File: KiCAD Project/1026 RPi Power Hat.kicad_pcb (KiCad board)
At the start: 4 copper layers, 85 x 56.5 mm, 131 parts, among them J1 S2B-XH-A-1, J2 B2B-XH-A(LF)(SN), J3 ESW-120-33-G-D, J4 USB1030-GF-P-B-B, J5 USB1035-GF-P-0-B-B, J6 USB1035-GF-P-0-B-B, M1 CFM-2507CF-050-089, P1 DW_PCB_Logo, P2 Raspberry Pi HAT+ Designator, Q1 BUK6D120-60PX, U1 LM64440APPQRYFRQ1, U10 USBLC6-2P6, U11 USBLC6-2P6, U12 USBLC6-2P6, U2 TLV75511PDQNR, U3 TLV75533PDQNR, U4 TUSB4041IPAPR, U5 TPS2561DRCR, U6 TPS2561DRCR, U7 CAT24C32HU4I-GT3, U8 USBLC6-2P6, U9 USBLC6-2P6, Y1 ECS-2520MV-240-BL-TR

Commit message: v1.0.0 RC2
Build candidate 2
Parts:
- M1: value CFM-2507CF-050-089 -> CFM-2510B-070-140; footprint DW_Mechanical:[Fan] SameSky CFM-2507CF-050-089 -> DW_Mechanical:[Fan] SameSky CFM-2510B-070-140
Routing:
- net /USB Hub/USB_Vbus: track 75.2 -> 78.9 mm, vias 1 -> 3
- net /5V Regulator/5V: track 15.4 -> 14.4 mm
- net GND: vias 92 -> 91
- added copper zone on In2.Cu, net /5V Regulator/24V
- removed copper zone on B.Cu, net /5V Regulator/24V
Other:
- board text added: "Fault"
- board text removed: "OC Fault"

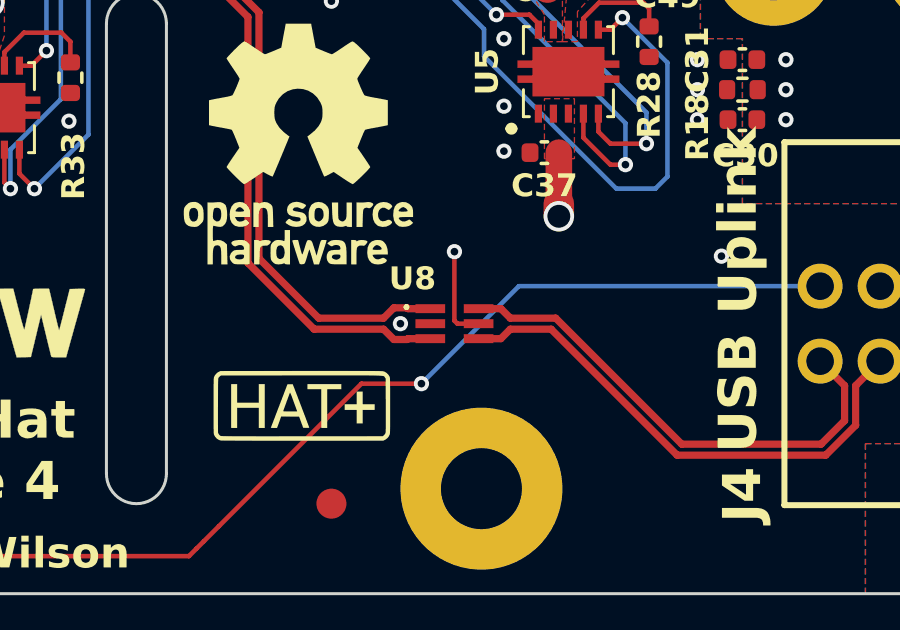
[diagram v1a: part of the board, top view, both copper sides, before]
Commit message: v1.0.0 RC3
Minor change to upstream USB port to connect Vbus to ESD protection vice on-board 5V.
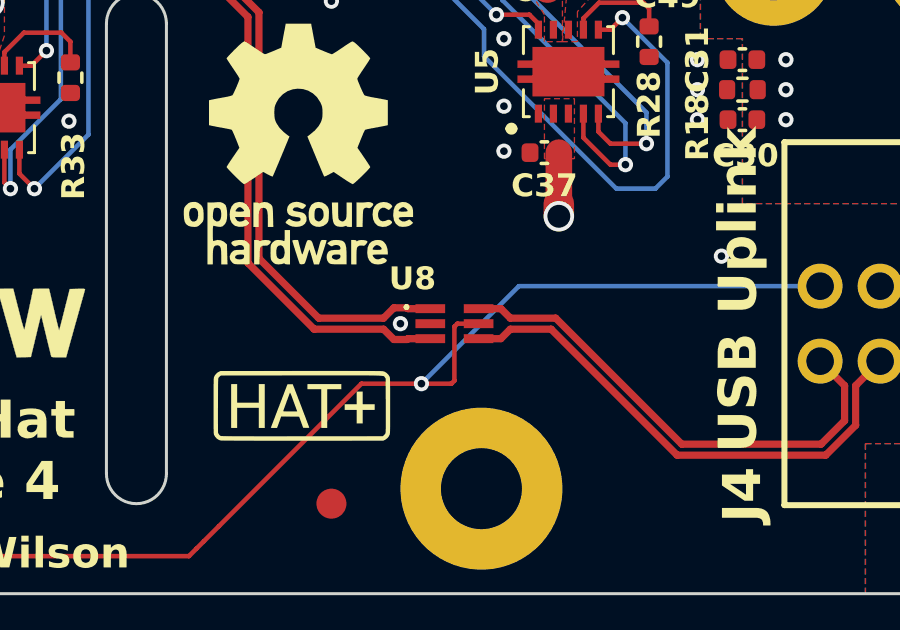
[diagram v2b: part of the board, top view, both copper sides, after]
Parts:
- C12: value GRM0225C1C100FA03L -> VJ0402A100GXJCW1BC
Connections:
- U8 pad 5: /5V Regulator/5V -> /USB Hub/USB_Vbus
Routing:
- net /USB Hub/USB_Vbus: track 78.9 -> 82.7 mm
- net /5V Regulator/5V: track 14.4 -> 11.2 mm, vias 26 -> 25
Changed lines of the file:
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@@
 		(title "1026 RPi Power Hat")
 		(date "2025-04-13")
-		(rev "1")
+		(rev "1.0.0 RC3")
 		(company "Dan Wilson")
 		(comment 1 "Copyright © 2025")
@@
 			)
 		)
-		(property "Spec" ""
+		(property "Spec" "CAT24C32HU4I-GT3"
 			(at 0 0 0)
 			(unlocked yes)
@@
 			)
 		)
-		(property "Value" "GRM0225C1C100FA03L"
+		(property "Value" "VJ0402A100GXJCW1BC"
 			(at 0 1.16 90)
 			(layer "F.Fab")
@@
 			)
 		)
-		(property "Datasheet" "https://www.mouser.com/datasheet/2/281/GRM0225C1C100FA03_01A-1978859.pdf"
+		(property "Datasheet" "https://www.vishay.com/doc?28548"
 			(at 0 0 270)
 			(unlocked yes)
@@
 			)
 		)
-		(property "Height" "0.25"
+		(property "Height" "0.5"
 			(at 0 0 270)
 			(unlocked yes)
@@
 			)
 		)
-		(property "Manufacturer_Name" "Murata"
+		(property "Manufacturer_Name" "Vishay"
 			(at 0 0 270)
 			(unlocked yes)
@@
 			)
 		)
-		(property "Manufacturer_Part_Number" "GRM0225C1C100FA03L"
+		(property "Manufacturer_Part_Number" "VJ0402A100GXJCW1BC"
 			(at 0 0 270)
 			(unlocked yes)
@@
 			)
 		)
-		(property "Mouser Part Number" "81-GRM0225C1C100FA03"
+		(property "Mouser Part Number" "77-VJ0402A100GXJCBC"
 			(at 0 0 270)
 			(unlocked yes)
@@
 			)
 		)
-		(property "Mouser Price/Stock" "https://www.mouser.com/ProductDetail/Murata-Electronics/GRM0225C1C100FA03L?qs=rrS6PyfT74dMR%2FKublCCEA%3D%3D"
+		(property "Mouser Price/Stock" "https://www.mouser.com/ProductDetail/77-VJ0402A100GXJCBC"
 			(at 0 0 270)
 			(unlocked yes)
@@
 			)
 		)
+		(property "Mouser Price/Stock" "https://www.mouser.com/ProductDetail/STMicroelectronics/USBLC6-2P6?qs=6ARB0lp6jlViGcbUSvj1Mw%3D%3D"
+			(at 0 0 270)
+			(unlocked yes)
+			(layer "F.Fab")
+			(hide yes)
+			(effects
+				(font
+					(size 1 1)
+					(thickness 0.15)
+				)
+			)
+		)
 		(sheetname "/USB ESD Protection/")
 		(sheetfile "USB ESD Protection.kicad_sch")
@@
 			)
 		)
+		(property "Spec" "TPS2561DRCR"
+			(at 0 0 90)
+			(unlocked yes)
+			(layer "F.Fab")
+			(hide yes)
+			(effects
+				(font
+					(size 1 1)
+					(thickness 0.15)
+				)
+			)
+		)
 		(sheetname "/USB Power Control/")
 		(sheetfile "USB Power Control.kicad_sch")
@@
 			)
 		)
+		(property "Mouser Price/Stock" "https://www.mouser.com/ProductDetail/STMicroelectronics/USBLC6-2P6?qs=6ARB0lp6jlViGcbUSvj1Mw%3D%3D"
+			(at 0 0 315)
+			(unlocked yes)
+			(layer "F.Fab")
+			(hide yes)
+			(effects
+				(font
+					(size 1 1)
+					(thickness 0.15)
+				)
+			)
+		)
 		(sheetname "/USB ESD Protection/")
 		(sheetfile "USB ESD Protection.kicad_sch")
@@
 			)
 		)
+		(property "Spec" "TPS2561DRCR"
+			(at 0 0 90)
+			(unlocked yes)
+			(layer "F.Fab")
+			(hide yes)
+			(effects
+				(font
+					(size 1 1)
+					(thickness 0.15)
+				)
+			)
+		)
 		(sheetname "/USB Power Control/")
 		(sheetfile "USB Power Control.kicad_sch")
@@
 			)
 		)
+		(property "Mouser Price/Stock" "https://www.mouser.com/ProductDetail/STMicroelectronics/USBLC6-2P6?qs=6ARB0lp6jlViGcbUSvj1Mw%3D%3D"
+			(at 0 0 315)
+			(unlocked yes)
+			(layer "F.Fab")
+			(hide yes)
+			(effects
+				(font
+					(size 1 1)
+					(thickness 0.15)
+				)
+			)
+		)
 		(sheetname "/USB ESD Protection/")
 		(sheetfile "USB ESD Protection.kicad_sch")
@@
 			)
 		)
-		(property "Mouser Part Number" ""
+		(property "Mouser Part Number" "306-B2BXHALFSNP"
 			(at 0 0 270)
 			(unlocked yes)
@@
 			)
 		)
+		(property "Mouser Price/Stock" "https://www.mouser.com/ProductDetail/JST-Commercial/B2B-XH-ALFSN?qs=cdbOS8ANM9DdcSn9qRmfCw%3D%3D"
+			(at 0 0 270)
+			(unlocked yes)
+			(layer "F.Fab")
+			(hide yes)
+			(effects
+				(font
+					(size 1 1)
+					(thickness 0.15)
+				)
+			)
+		)
 		(sheetname "/Fan / Header / GPIO / EEPROM/")
 		(sheetfile "Fan Header and Fan.kicad_sch")
@@
 			)
 		)
+		(property "Mouser Price/Stock" "https://www.mouser.com/ProductDetail/STMicroelectronics/USBLC6-2P6?qs=6ARB0lp6jlViGcbUSvj1Mw%3D%3D"
+			(at 0 0 270)
+			(unlocked yes)
+			(layer "F.Fab")
+			(hide yes)
+			(effects
+				(font
+					(size 1 1)
+					(thickness 0.15)
+				)
+			)
+		)
 		(sheetname "/USB ESD Protection/")
 		(sheetfile "USB ESD Protection.kicad_sch")
@@
 			(size 0.3 0.99)
 			(layers "F.Cu" "F.Mask" "F.Paste")
-			(net 7 "/5V Regulator/5V")
+			(net 90 "/USB Hub/USB_Vbus")
 			(pinfunction "VBUS")
 			(pintype "passive")
@@
 			)
 		)
-		(property "Mouser Part Number" ""
+		(property "Mouser Part Number" "306-S2BXHA1LFSN"
 			(at 0 0 180)
 			(unlocked yes)
@@
 			)
 		)
+		(property "Mouser Price/Stock" "https://www.mouser.com/ProductDetail/JST-Commercial/S2B-XH-A-1LFSN?qs=QpmGXVUTftHhNeC%252BPQWeTw%3D%3D"
+			(at 0 0 180)
+			(unlocked yes)
+			(layer "F.Fab")
+			(hide yes)
+			(effects
+				(font
+					(size 1 1)
+					(thickness 0.15)
+				)
+			)
+		)
 		(sheetname "/Power Input/")
 		(sheetfile "Power Input.kicad_sch")
@@
 			)
 		)
+		(property "Spec" "ECS-2520MV-240-BL-TR"
+			(at 0 0 135)
+			(unlocked yes)
+			(layer "F.Fab")
+			(hide yes)
+			(effects
+				(font
+					(size 1 1)
+					(thickness 0.15)
+				)
+			)
+		)
 		(sheetname "/USB Power Control/")
 		(sheetfile "USB Power Control.kicad_sch")
@@
 			)
 		)
+		(property "Spec" "5V 7000RPM 25mm"
+			(at 0 0 180)
+			(unlocked yes)
+			(layer "F.Fab")
+			(hide yes)
+			(effects
+				(font
+					(size 1 1)
+					(thickness 0.15)
+				)
+			)
+		)
 		(sheetname "/Fan / Header / GPIO / EEPROM/")
 		(sheetfile "Fan Header and Fan.kicad_sch")
@@
 			)
 		)
+		(property "Mouser Price/Stock" "https://www.mouser.com/ProductDetail/STMicroelectronics/USBLC6-2P6?qs=6ARB0lp6jlViGcbUSvj1Mw%3D%3D"
+			(at 0 0 315)
+			(unlocked yes)
+			(layer "F.Fab")
+			(hide yes)
+			(effects
+				(font
+					(size 1 1)
+					(thickness 0.15)
+				)
+			)
+		)
 		(sheetname "/USB ESD Protection/")
 		(sheetfile "USB ESD Protection.kicad_sch")
@@
 			)
 		)
+		(property "Spec" "TUSB4041IPAPR"
+			(at 0 0 315)
+			(unlocked yes)
+			(layer "F.Fab")
+			(hide yes)
+			(effects
+				(font
+					(size 1 1)
+					(thickness 0.15)
+				)
+			)
+		)
 		(sheetname "/USB Hub/")
 		(sheetfile "USB Hub and Power Control.kicad_sch")
@@
 	)
 	(segment
-		(start 160.6992 141)
-		(end 160.6 140.9008)
-		(width 0.1524)
-		(layer "F.Cu")
-		(net 7)
-	)
-	(segment
 		(start 125.74 143.99)
 		(end 125.75 144)
@@
 	)
 	(segment
-		(start 160.6 140.9008)
-		(end 160.6 138.6)
-		(width 0.1524)
-		(layer "F.Cu")
-		(net 7)
-	)
-	(segment
 		(start 123 140.26)
 		(end 123 142.75)
@@
 		(net 7)
 	)
-	(segment
-		(start 161.405 141)
-		(end 160.6992 141)
-		(width 0.1524)
-		(layer "F.Cu")
-		(net 7)
-	)
 	(via
 		(at 123 142.75)
@@
 	)
 	(via
-		(at 160.6 138.6)
-		(size 0.508)
-		(drill 0.254)
-		(layers "F.Cu" "B.Cu")
-		(net 7)
-	)
-	(via
 		(at 121.5 130.25)
 		(size 0.508)
@@
 	)
 	(segment
+		(start 160.6992 141)
+		(end 161.405 141)
+		(width 0.1524)
+		(layer "F.Cu")
+		(net 90)
+	)
+	(segment
 		(start 152.25 148.25)
 		(end 152 148.5)
@@
 	)
 	(segment
+		(start 160.6 142.9)
+		(end 160.6 141.0992)
+		(width 0.1524)
+		(layer "F.Cu")
+		(net 90)
+	)
+	(segment
 		(start 139 146.25)
 		(end 139 136)
@@
 	)
 	(segment
+		(start 159.5 143)
+		(end 160.5 143)
+		(width 0.1524)
+		(layer "F.Cu")
+		(net 90)
+	)
+	(segment
 		(start 152 148.5)
 		(end 151.75 148.75)
@@
 	)
 	(segment
+		(start 160.6 141.0992)
+		(end 160.6992 141)
+		(width 0.1524)
+		(layer "F.Cu")
+		(net 90)
+	)
+	(segment
 		(start 159.5 143)
 		(end 157.5 143)
@@
 		(width 0.1524)
 		(layer "F.Cu")
+		(net 90)
+	)
+	(segment
+		(start 160.5 143)
+		(end 160.6 142.9)
+		(width 0.1524)
+		(layer "F.Cu")

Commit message: v1.0.0
Initial Commit
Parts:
- added G2: OSHW_Logo, DW_Mechanical:OSHW_Logo, B.Cu at (136.0, 136.0)
- H1, H4: footprint DW_Mechanical:[MH] MountingHole_2.7mm_M2.5_Pad_StencilRegHole -> DW_Mechanical:[MH] MountingHole_2.7mm_M2.5
- H2, H3: footprint DW_Mechanical:[MH] MountingHole_2.7mm_M2.5_Pad -> DW_Mechanical:[MH] MountingHole_2.7mm_M2.5_StencilRegHole
- moved H2 58.0 mm to (161.5, 97.5)
- moved H3 58.0 mm to (103.5, 146.5)
- moved H1 49.0 mm to (103.5, 97.5)
- moved H4 49.0 mm to (161.5, 146.5)
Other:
- board text added: "This device's design is licensed under the CERN Open Hardware License v2, Weakly Reciprocal: https://ohwr.org/cern_ohl_w_v2.txt"

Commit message: v1.0.0A
Moved all symbols, footprints, and 3D models to local project-specific libraries in /KiCAD Project/Libraries.
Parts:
- C1, C2: footprint DW_Passives:[C] Kemet Tantalum Polymer T521X -> 1026-3D:[C] Kemet Tantalum Polymer T521X
- C10, C11, C3, C4: footprint Capacitor_SMD:C_1210_3225Metric -> 1026-3D:C_1210_3225Metric
- C12, C17, C18, C19, C20, C22, C23, C24, C25, C26, C27, C28, C30, C31, C32, C33, C34, C35, C37, C38, C39, C42, C43, C45, C47, C48, C49, C5, C50, C51, C52, C6, C8, C9: footprint Capacitor_SMD:C_0402_1005Metric -> 1026-3D:C_0402_1005Metric
- C13, C14, C15, C16, C36, C7: footprint Capacitor_SMD:C_0603_1608Metric -> 1026-3D:C_0603_1608Metric
- C21, C29: footprint Capacitor_SMD:C_0805_2012Metric -> 1026-3D:C_0805_2012Metric
- C40, C41, C44, C46: footprint DW_Passives:[C] Kyocera AVC Tant Poly TCJB157M006R0070 -> 1026-3D:[C] Kyocera AVC Tant Poly TCJB157M006R0070
- D1: footprint DW_Semiconductors:[D] Nexperia Zener PDZ10B,115 10V -> 1026-3D:[D] Nexperia Zener PDZ10B,115 10V
- D2: footprint DW_Optoelectronics:[D] Wurth Elektronik 150040GS73220 -> 1026-3D:[D] Wurth Elektronik 150040GS73220
- D3: footprint DW_CircuitProtection:[D] Littelfuse SMF24CA 24V 200W -> 1026-3D:[D] Littelfuse SMF24CA 24V 200W
- D4: footprint DW_Optoelectronics:[D] Wurth Elektronik 150040RS73240 -> 1026-3D:[D] Wurth Elektronik 150040RS73240
- F1: footprint DW_CircuitProtection:[F] Littelfuse PPTC 1812L010DR -> 1026-3D:[F] Littelfuse PPTC 1812L010DR
- FB1, FB2: footprint DW_Passives:[FB] Murata BLM15PX221SZ1D -> 1026-3D:[FB] Murata BLM15PX221SZ1D
- FB3, FB4, FB5, FB6: footprint DW_Passives:[FB] Murata BLM18KG221SN1D 220ohm 2.2A -> 1026-3D:[FB] Murata BLM18KG221SN1D 220ohm 2.2A
- FID1, FID2, FID3: footprint Fiducial:Fiducial_1mm_Mask2mm -> 1026-3D:Fiducial_1mm_Mask2mm
- G1, G2: footprint DW_Mechanical:OSHW_Logo -> 1026-3D:OSHW_Logo
- H1, H4: footprint DW_Mechanical:[MH] MountingHole_2.7mm_M2.5 -> 1026-3D:[MH] MountingHole_2.7mm_M2.5
- H2, H3: footprint DW_Mechanical:[MH] MountingHole_2.7mm_M2.5_StencilRegHole -> 1026-3D:[MH] MountingHole_2.7mm_M2.5_StencilRegHole
- J1: footprint DW_Connectors:[J] JST S2B-XH-A-1 -> 1026-3D:[J] JST S2B-XH-A-1
- J2: footprint DW_Connectors:JST_B2B-XH-A(LF)(SN) -> 1026-3D:JST_B2B-XH-A(LF)(SN)
- J3: footprint DW_Connectors:[J] Samtec Elevated Socket Strip ESW-120-33-G-D -> 1026-3D:[J] Samtec Elevated Socket Strip ESW-120-33-G-D
- J4: footprint DW_Connectors:[J] GCT USB-B 2.0 Connector PCB USB1030-GF-P-B-B -> 1026-3D:[J] GCT USB-B 2.0 Connector PCB USB1030-GF-P-B-B
- J5, J6: footprint DW_Connectors:[J] GCT USB-A x2 2.0 Connector USB1035-GF-P-0-B-B -> 1026-3D:[J] GCT USB-A x2 2.0 Connector USB1035-GF-P-0-B-B
- L1: footprint DW_Passives:[L] Coilcraft Inductor LPS4040 -> 1026-3D:[L] Coilcraft Inductor LPS4040
- L2: footprint DW_Passives:[L] Coilcraft Inductor XGL4025 -> 1026-3D:[L] Coilcraft Inductor XGL4025
- M1: footprint DW_Mechanical:[Fan] SameSky CFM-2510B-070-140 -> 1026-3D:[Fan] SameSky CFM-2510B-070-140
- P1: footprint DW_Mechanical:DW_PCB_Logo -> 1026-3D:DW_PCB_Logo
- P2: footprint DW_Mechanical:[G] RPi HAT+ Designator -> 1026-3D:[G] RPi HAT+ Designator
- Q1: footprint DW_Semiconductors:[Q] Nexperia BUK6D120-60PX P-Ch 60V 8A -> 1026-3D:[Q] Nexperia BUK6D120-60PX P-Ch 60V 8A
- R1, R10, R11, R12, R13, R14, R15, R16, R17, R18, R19, R2, R20, R21, R22, R23, R24, R25, R26, R27, R28, R29, R3, R30, R31, R32, R33, R34, R35, R4, R5, R6, R7, R8, R9: footprint Resistor_SMD:R_0402_1005Metric -> 1026-3D:R_0402_1005Metric
- U1: footprint DW_Semiconductors:[U] TI LM63460 Sw Volt Reg -> 1026-3D:[U] TI LM63460 Sw Volt Reg
- U10, U11, U12, U8, U9: footprint DW_Semiconductors:[U] ST Micro USB ESD Protection USBLC6-2P6 -> 1026-3D:[U] ST Micro USB ESD Protection USBLC6-2P6
- U2, U3: footprint DW_Semiconductors:[U] TI LDO Regulator TLV755 DQN -> 1026-3D:[U] TI LDO Regulator TLV755 DQN
- U4: footprint DW_Semiconductors:[U] Texas Inst USB 2.0 Hub Controller TUSB4041I QFP50P1200X1200X120-65N -> 1026-3D:[U] Texas Inst USB 2.0 Hub Controller TUSB4041I QFP50P1200X1200X120-65N
- U5, U6: footprint DW_Semiconductors:[U] TI USB Power Ctlr TPS2561DRCR -> 1026-3D:[U] TI USB Power Ctlr TPS2561DRCR
- U7: footprint DW_Semiconductors:[U] OnSemi Serial EEPROM 4KB CAT24C32HU4I-GT3 -> 1026-3D:[U] OnSemi Serial EEPROM 4KB CAT24C32HU4I-GT3
- Y1: footprint DW_Semiconductors:[Y] ECS Clock Osc 24MHz ECS2520MV240BLTR -> 1026-3D:[Y] ECS Clock Osc 24MHz ECS2520MV240BLTR

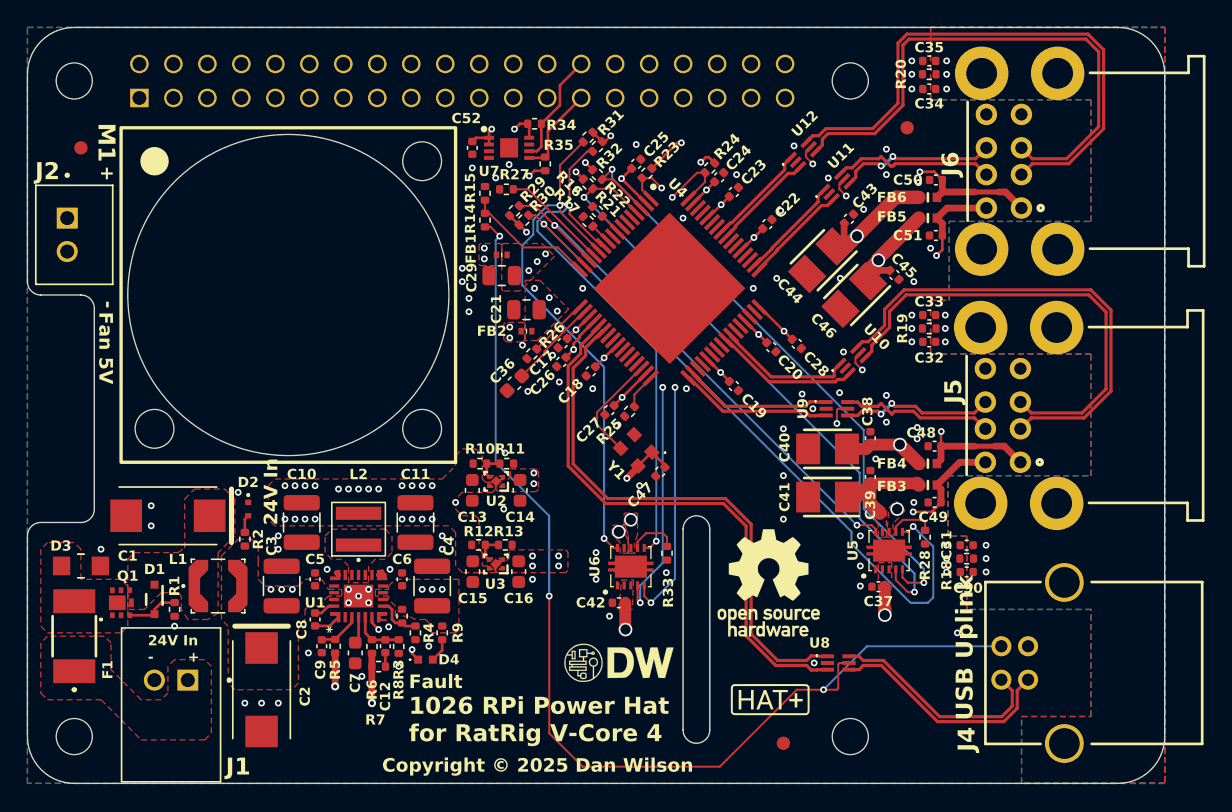
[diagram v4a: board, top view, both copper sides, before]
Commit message: Solder mask, parts and text updates
Use pass through header ESW-120-34-G-D vs ESW-120-33-G-D
Add PCBWay test WayWayWay under J4
Change board name text to be "1026 RPi Power Hat"
Add board version text "1.0.0 Rev A"
Change Solder Mask clearance from 0 to -0.01 on U4 in footprint properties for PCBway minimum clearance of 0.22mm
Change board silkscreen color to Black
Remove references to unused Jua font
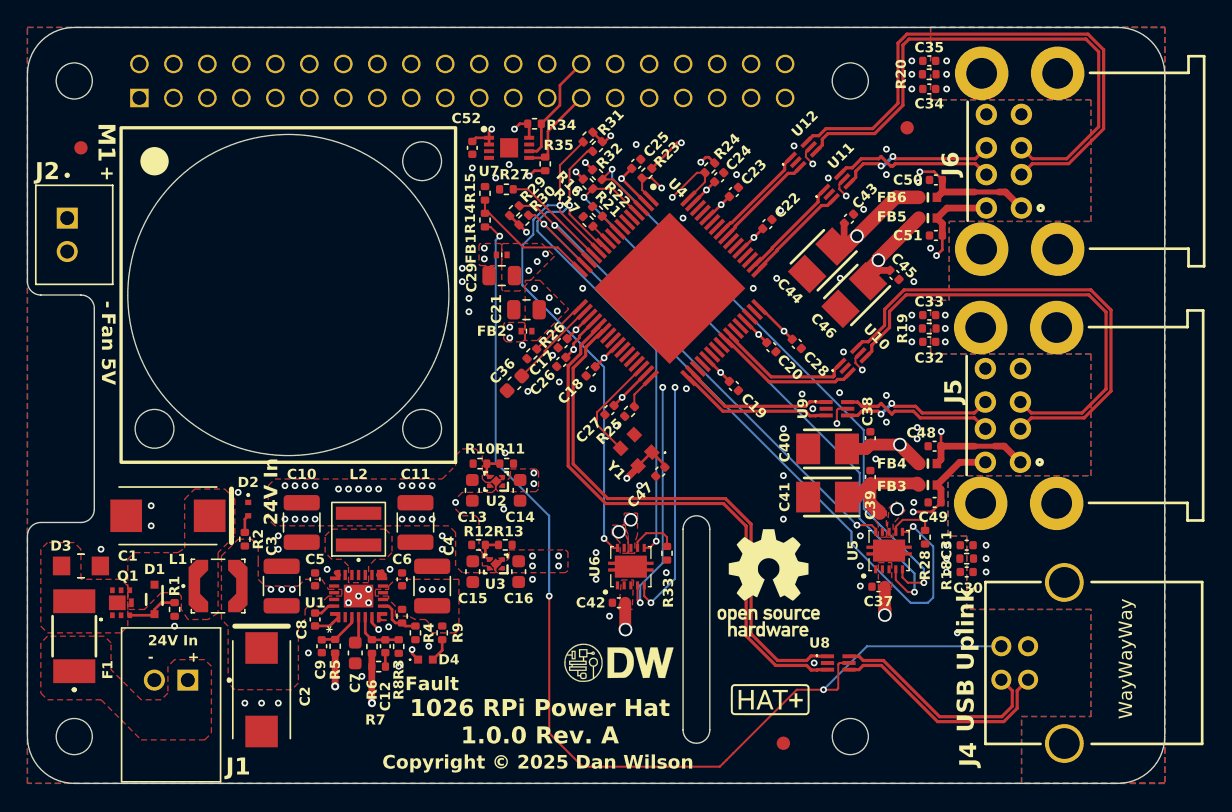
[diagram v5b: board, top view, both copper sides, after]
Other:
- rule pad_to_mask_clearance: 0.0254 -> 0
- board text added: "1026 RPi Power Hat 1.0.0 Rev. A"
- board text added: "WayWayWay"
- board text removed: "1026 RPi Power Hat for RatRig V-Core 4"
